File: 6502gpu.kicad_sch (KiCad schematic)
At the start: 13 parts, among them J1 Conn_01x02, J2 Conn_01x08, J3 Conn_01x02, J4 Conn_01x16, J5 Conn_01x01, J6 Conn_01x03, J7 DE15_Receptacle_HighDensity, J8 Conn_01x02, J9 Conn_01x02, U1 74HC86, U2 74HC00, U3 74LV27

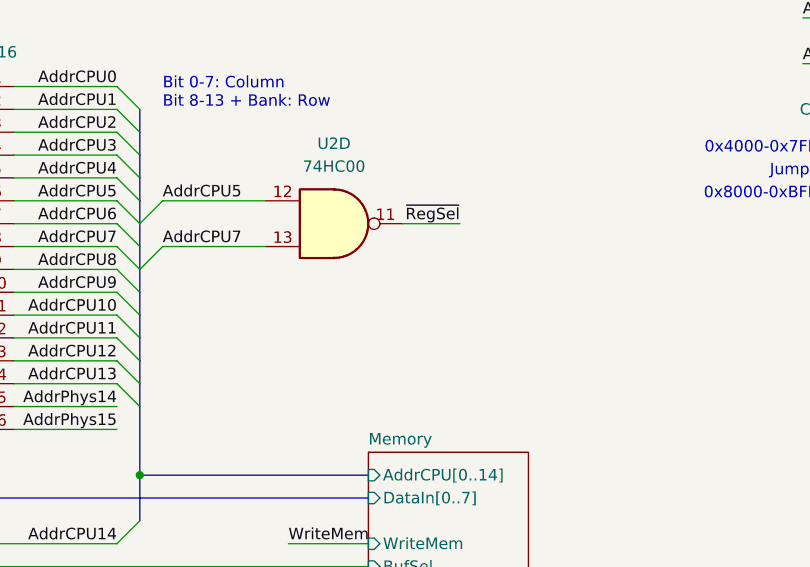
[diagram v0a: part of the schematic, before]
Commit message: Fix some timing, simulate writing to memory
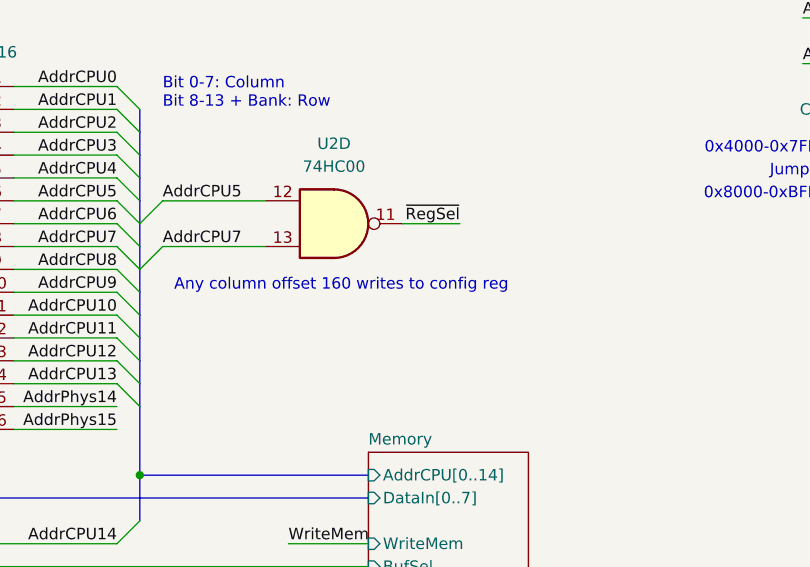
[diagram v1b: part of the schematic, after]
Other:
- note added: "Any column offset 160 writes to config reg"
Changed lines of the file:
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@@
     (stroke (width 0) (type default))
+  )
+  (text "Any column offset 160 writes to config reg" (at 93.98 73.66 0)
+    (effects (font (size 1.27 1.27)) (justify left bottom))
   )
   (text "Green" (at 177.8 124.46 0)

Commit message: pcb organization
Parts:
- removed J8, J9: Conn_01x02, Connector_PinHeader_2.54mm:PinHeader_1x02_P2.54mm_Vertical, symbol Connector_Generic:Conn_01x02
- added J15: Conn_01x03, Connector_PinHeader_2.54mm:PinHeader_1x03_P2.54mm_Vertical, symbol Connector_Generic:Conn_01x03
- added J8: Conn_01x08, Connector_PinHeader_2.54mm:PinHeader_1x08_P2.54mm_Vertical, symbol Connector_Generic:Conn_01x08
- J5: value Conn_01x01 -> Conn_01x02; footprint Connector_PinHeader_2.54mm:PinHeader_1x01_P2.54mm_Vertical -> Connector_PinHeader_2.54mm:PinHeader_1x02_P2.54mm_Vertical; symbol Connector_Generic:Conn_01x01 -> Connector_Generic:Conn_01x02
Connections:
- net ~{HSync}: now also J7.13
- net ~{VSync}: now also J7.14
- net Counters/HBlank renamed HBlank
- net Counters/VBlank renamed VBlank
- net DAC/Blue renamed Blue
- net Blue: now also J15.3 (Pin_3)
- net DAC/Green renamed Green
- net Green: now also J15.2 (Pin_2)
- net DAC/Red renamed Red
- net Red: now also J15.1 (Pin_1)
- net ~{EnableCPU} renamed ~{FbSelected}
- net ~{FbSelected}: now also J5.2 (Pin_2)
- new net PixelOut0: J8.1 (Pin_1)
- new net PixelOut1: J8.2 (Pin_2)
- new net PixelOut2: J8.3 (Pin_3)
- new net PixelOut3: J8.4 (Pin_4)
- new net PixelOut4: J8.5 (Pin_5)
- new net PixelOut5: J8.6 (Pin_6)
- new net PixelOut6: J8.7 (Pin_7)
- new net PixelOut7: J8.8 (Pin_8)
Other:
- note removed: "Blue"
- note removed: "Green"
- note removed: "Red"
- moved on the sheet: J6, J7, U1A, U1C, U2B, U3B, U3C

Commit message: Routing work
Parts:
- J7: footprint footprints:CONN_L77HDE15SD1CH4FVGA_AMP -> Connector_Dsub:DSUB-15-HD_Female_Horizontal_P2.29x1.98mm_EdgePinOffset8.35mm_Housed_MountingHolesOffset10.89mm
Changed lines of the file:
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@@
       (effects (font (size 1.27 1.27)))
     )
-    (property "Footprint" "footprints:CONN_L77HDE15SD1CH4FVGA_AMP" (at 168.91 119.38 0)
+    (property "Footprint" "Connector_Dsub:DSUB-15-HD_Female_Horizontal_P2.29x1.98mm_EdgePinOffset8.35mm_Housed_MountingHolesOffset10.89mm" (at 168.91 119.38 0)
       (effects (font (size 1.27 1.27)) hide)
     )

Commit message: layout continues...
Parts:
- added J17: Barrel_Jack, Connector_BarrelJack:BarrelJack_CUI_PJ-102AH_Horizontal, symbol Connector:Barrel_Jack_Switch
- added SW1: SW_SPST, symbol Switch:SW_SPST
- added U34: LM7805, Package_TO_SOT_THT:TO-220-3_Vertical, symbol Regulator_Linear:LM7805_TO220
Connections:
- net +5V: now also SW1.2 (B)
- net GND: now also J17.2, J17.3, U34.2 (GND)
- new net: J17.1, U34.1 (VI)
- new net: SW1.1 (A), U34.3 (VO)
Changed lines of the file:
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@@
   (junction (at 177.8 137.16) (diameter 0) (color 0 0 0 0)
   )
+  (junction (at 115.57 26.67) (diameter 0) (color 0 0 0 0)
+  )
   (junction (at 135.89 114.3) (diameter 0) (color 0 0 0 0)
   )
   (junction (at 118.11 191.77) (diameter 0) (color 0 0 0 0)
   )
+  (junction (at 95.25 34.29) (diameter 0) (color 0 0 0 0)
+  )
   (junction (at 110.49 127) (diameter 0) (color 0 0 0 0)
   )
@@
   )
   (junction (at 34.29 45.72) (diameter 0) (color 0 0 0 0)
+  )
+  (junction (at 87.63 31.75) (diameter 0) (color 0 0 0 0)
   )
   (junction (at 177.8 139.7) (diameter 0) (color 0 0 0 0)
@@
     (stroke (width 0) (type default))
   )
+  (wire (pts (xy 87.63 29.21) (xy 87.63 31.75))
+    (stroke (width 0) (type default))
+  )
   (bus (pts (xy 90.17 68.58) (xy 90.17 71.12))
     (stroke (width 0) (type default))
@@
     (stroke (width 0) (type default))
   )
+  (wire (pts (xy 115.57 26.67) (xy 123.19 26.67))
+    (stroke (width 0) (type default))
+  )
   (wire (pts (xy 96.52 186.69) (xy 96.52 191.77))
     (stroke (width 0) (type default))
@@
     (stroke (width 0) (type default))
   )
+  (wire (pts (xy 87.63 34.29) (xy 95.25 34.29))
+    (stroke (width 0) (type default))
+  )
   (wire (pts (xy 110.49 127) (xy 110.49 143.51))
     (stroke (width 0) (type default))
@@
     (stroke (width 0) (type default))
   )
+  (wire (pts (xy 87.63 31.75) (xy 87.63 34.29))
+    (stroke (width 0) (type default))
+  )
   (wire (pts (xy 76.2 86.36) (xy 87.63 86.36))
     (stroke (width 0) (type default))
@@
   )
   (wire (pts (xy 110.49 127) (xy 137.16 127))
+    (stroke (width 0) (type default))
+  )
+  (wire (pts (xy 113.03 26.67) (xy 115.57 26.67))
     (stroke (width 0) (type default))
   )
@@
     )
   )
+  (symbol (lib_id "power:+5V") (at 115.57 26.67 0) (unit 1)
+    (in_bom yes) (on_board yes) (dnp no) (fields_autoplaced)
+    (property "Reference" "#PWR0108" (at 115.57 30.48 0)
+      (effects (font (size 1.27 1.27)) hide)
+    )
+    (property "Value" "+5V" (at 115.57 21.59 0)
+      (effects (font (size 1.27 1.27)))
+    )
+    (property "Footprint" "" (at 115.57 26.67 0)
+      (effects (font (size 1.27 1.27)) hide)
+    )
+    (property "Datasheet" "" (at 115.57 26.67 0)
+      (effects (font (size 1.27 1.27)) hide)
+    )
+    (pin "1")
+    (instances
+      (project "6502gpu"
+        (path "/b1d8dca2-c863-4452-b293-53802be895cc"
+          (reference "#PWR0108") (unit 1)
+        )
+      )
+    )
+  )
   (symbol (lib_id "Connector_Generic:Conn_01x03") (at 195.58 59.69 0) (mirror y) (unit 1)
     (in_bom yes) (on_board yes) (dnp no) (fields_autoplaced)
@@
         (path "/b1d8dca2-c863-4452-b293-53802be895cc"
           (reference "C35") (unit 1)
+        )
+      )
+    )
+  )
+  (symbol (lib_id "power:GND") (at 95.25 34.29 0) (unit 1)
+    (in_bom yes) (on_board yes) (dnp no) (fields_autoplaced)
+    (property "Reference" "#PWR0107" (at 95.25 40.64 0)
+      (effects (font (size 1.27 1.27)) hide)
+    )
+    (property "Value" "GND" (at 95.25 39.37 0)
+      (effects (font (size 1.27 1.27)))
+    )
+    (property "Footprint" "" (at 95.25 34.29 0)
+      (effects (font (size 1.27 1.27)) hide)
+    )
+    (property "Datasheet" "" (at 95.25 34.29 0)
+      (effects (font (size 1.27 1.27)) hide)
+    )
+    (pin "1")
+    (instances
+      (project "6502gpu"
+        (path "/b1d8dca2-c863-4452-b293-53802be895cc"
+          (reference "#PWR0107") (unit 1)
         )
       )
@@
     )
   )
+  (symbol (lib_id "Regulator_Linear:LM7805_TO220") (at 95.25 26.67 0) (unit 1)
+    (in_bom yes) (on_board yes) (dnp no) (fields_autoplaced)
+    (property "Reference" "U34" (at 95.25 20.32 0)
+      (effects (font (size 1.27 1.27)))
+    )
+    (property "Value" "LM7805" (at 95.25 22.86 0)
+      (effects (font (size 1.27 1.27)))
+    )
+    (property "Footprint" "Package_TO_SOT_THT:TO-220-3_Vertical" (at 95.25 20.955 0)
+      (effects (font (size 1.27 1.27) italic) hide)
+    )
+    (property "Datasheet" "https://www.onsemi.cn/PowerSolutions/document/MC7800-D.PDF" (at 95.25 27.94 0)
+      (effects (font (size 1.27 1.27)) hide)
+    )
+    (pin "1")
+    (pin "2")
+    (pin "3")
+    (instances
+      (project "6502gpu"
+        (path "/b1d8dca2-c863-4452-b293-53802be895cc"
+          (reference "U34") (unit 1)
+        )
+      )
+    )
+  )
   (symbol (lib_id "Connector_Generic:Conn_01x02") (at 26.67 31.75 0) (mirror y) (unit 1)
     (in_bom yes) (on_board yes) (dnp no)
@@
         (path "/b1d8dca2-c863-4452-b293-53802be895cc"
           (reference "J1") (unit 1)
+        )
+      )
+    )
+  )
+  (symbol (lib_id "Connector:Barrel_Jack_Switch") (at 80.01 29.21 0) (unit 1)
+    (in_bom yes) (on_board yes) (dnp no) (fields_autoplaced)
+    (property "Reference" "J17" (at 80.01 20.32 0)
+      (effects (font (size 1.27 1.27)))
+    )
+    (property "Value" "Barrel_Jack" (at 80.01 22.86 0)
+      (effects (font (size 1.27 1.27)))
+    )
+    (property "Footprint" "Connector_BarrelJack:BarrelJack_CUI_PJ-102AH_Horizontal" (at 81.28 30.226 0)
+      (effects (font (size 1.27 1.27)) hide)
+    )
+    (property "Datasheet" "~" (at 81.28 30.226 0)
+      (effects (font (size 1.27 1.27)) hide)
+    )
+    (pin "1")
+    (pin "2")
+    (pin "3")
+    (instances
+      (project "6502gpu"
+        (path "/b1d8dca2-c863-4452-b293-53802be895cc"
+          (reference "J17") (unit 1)
         )
       )
@@
         (path "/b1d8dca2-c863-4452-b293-53802be895cc"
           (reference "U3") (unit 3)
+        )
+      )
+    )
+  )
+  (symbol (lib_id "Switch:SW_SPST") (at 107.95 26.67 0) (unit 1)
+    (in_bom yes) (on_board yes) (dnp no) (fields_autoplaced)
+    (property "Reference" "SW1" (at 107.95 20.32 0)
+      (effects (font (size 1.27 1.27)))
+    )
+    (property "Value" "SW_SPST" (at 107.95 22.86 0)
+      (effects (font (size 1.27 1.27)))
+    )
+    (property "Footprint" "" (at 107.95 26.67 0)
+      (effects (font (size 1.27 1.27)) hide)
+    )
+    (property "Datasheet" "~" (at 107.95 26.67 0)
+      (effects (font (size 1.27 1.27)) hide)
+    )
+    (pin "1")
+    (pin "2")
+    (instances
+      (project "6502gpu"
+        (path "/b1d8dca2-c863-4452-b293-53802be895cc"
+          (reference "SW1") (unit 1)
         )
       )
@@
         )
       )
+    )
+  )
+  (symbol (lib_id "power:PWR_FLAG") (at 123.19 26.67 0) (unit 1)
+    (in_bom yes) (on_board yes) (dnp no) (fields_autoplaced)
+    (property "Reference" "#FLG03" (at 123.19 24.765 0)
+      (effects (font (size 1.27 1.27)) hide)
+    )
+    (property "Value" "PWR_FLAG" (at 123.19 21.59 0)
+      (effects (font (size 1.27 1.27)))
+    )
+    (property "Footprint" "" (at 123.19 26.67 0)
+      (effects (font (size 1.27 1.27)) hide)
+    )
+    (property "Datasheet" "~" (at 123.19 26.67 0)
+      (effects (font (size 1.27 1.27)) hide)
+    )
+    (pin "1")
+    (instances
+      (project "6502gpu"
+        (path "/b1d8dca2-c863-4452-b293-53802be895cc"
+          (reference "#FLG03") (unit 1)
+        )
+      )

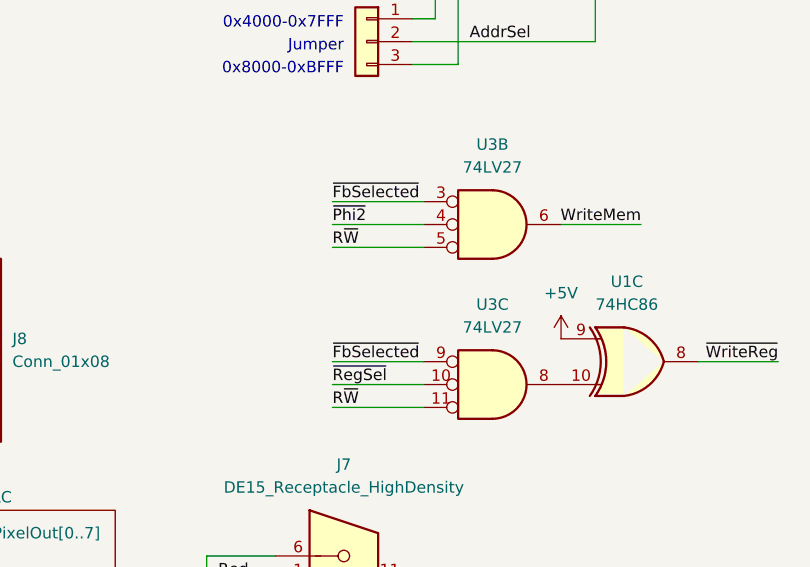
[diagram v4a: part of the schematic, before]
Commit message: finalize board layout at 140x110mm
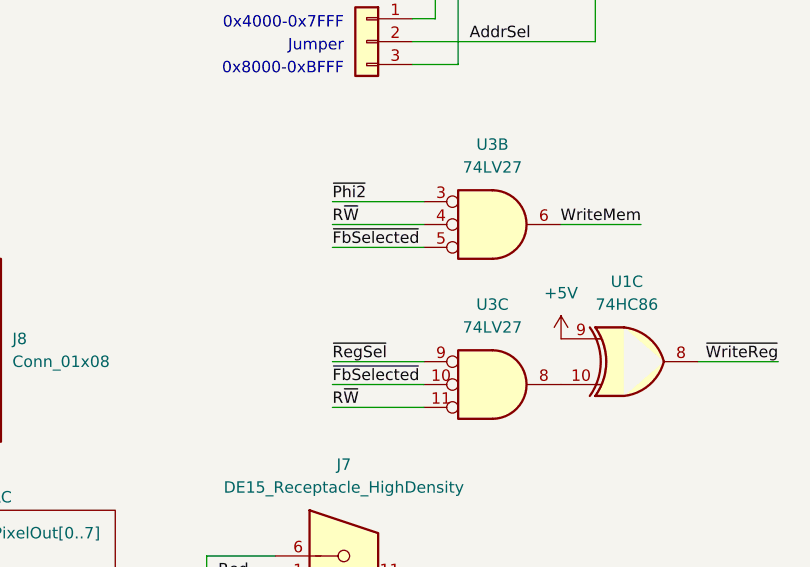
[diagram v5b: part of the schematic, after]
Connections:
- net R~{W}: now also U3.4; no longer U3.5
- net ~{FbSelected}: now also U3.10, U3.5; no longer U3.3, U3.9
- net ~{Phi2}: now also U3.3; no longer U3.4
- net ~{RegSel}: now also U3.9; no longer U3.10
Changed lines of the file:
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@@
     (effects (font (size 1.27 1.27)) (justify right bottom))
   )
-  (label "R~{W}" (at 191.77 82.55 0) (fields_autoplaced)
+  (label "R~{W}" (at 191.77 80.01 0) (fields_autoplaced)
     (effects (font (size 1.27 1.27)) (justify left bottom))
   )
@@
     (effects (font (size 1.27 1.27)) (justify left bottom))
   )
-  (label "~{FbSelected}" (at 191.77 77.47 0) (fields_autoplaced)
+  (label "~{FbSelected}" (at 191.77 82.55 0) (fields_autoplaced)
     (effects (font (size 1.27 1.27)) (justify left bottom))
   )
@@
     (effects (font (size 1.27 1.27)) (justify left bottom))
   )
-  (label "~{Phi2}" (at 191.77 80.01 0) (fields_autoplaced)
+  (label "~{Phi2}" (at 191.77 77.47 0) (fields_autoplaced)
     (effects (font (size 1.27 1.27)) (justify left bottom))
   )
@@
     (effects (font (size 1.27 1.27)) (justify right bottom))
   )
-  (label "~{FbSelected}" (at 191.77 95.25 0) (fields_autoplaced)
+  (label "~{FbSelected}" (at 191.77 97.79 0) (fields_autoplaced)
     (effects (font (size 1.27 1.27)) (justify left bottom))
   )
@@
     (effects (font (size 1.27 1.27)) (justify right bottom))
   )
-  (label "~{RegSel}" (at 191.77 97.79 0) (fields_autoplaced)
+  (label "~{RegSel}" (at 191.77 95.25 0) (fields_autoplaced)
     (effects (font (size 1.27 1.27)) (justify left bottom))
   )
